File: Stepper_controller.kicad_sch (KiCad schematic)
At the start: 26 parts

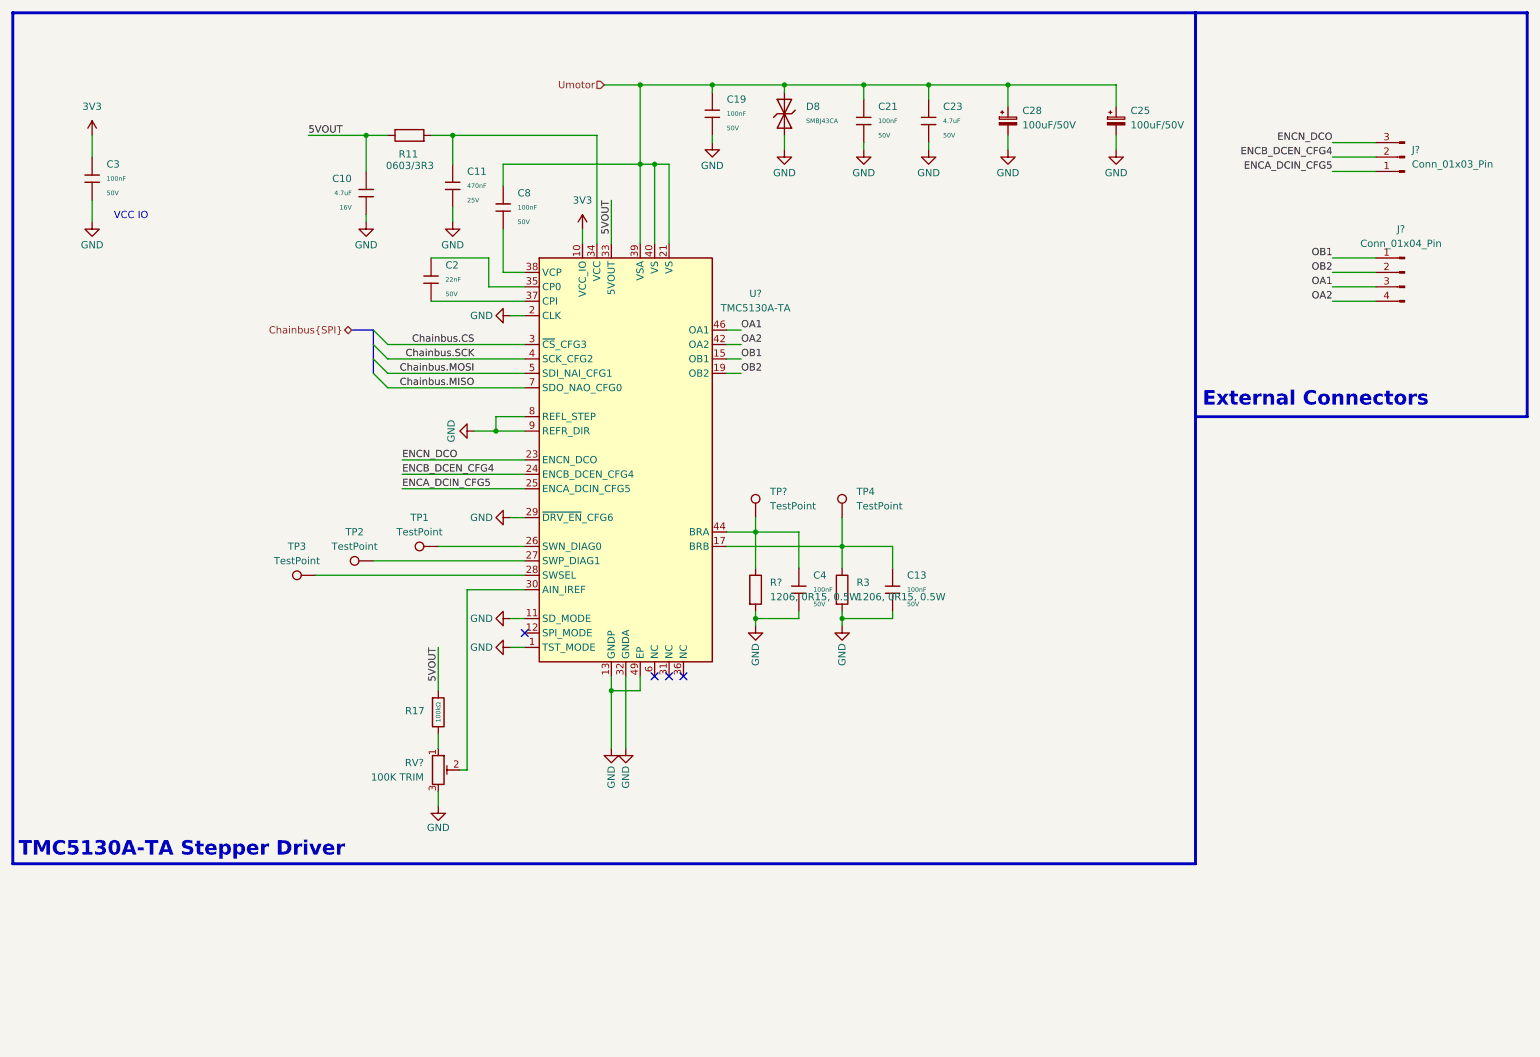
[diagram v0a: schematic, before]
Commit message: finished schematic (without some part numbers)
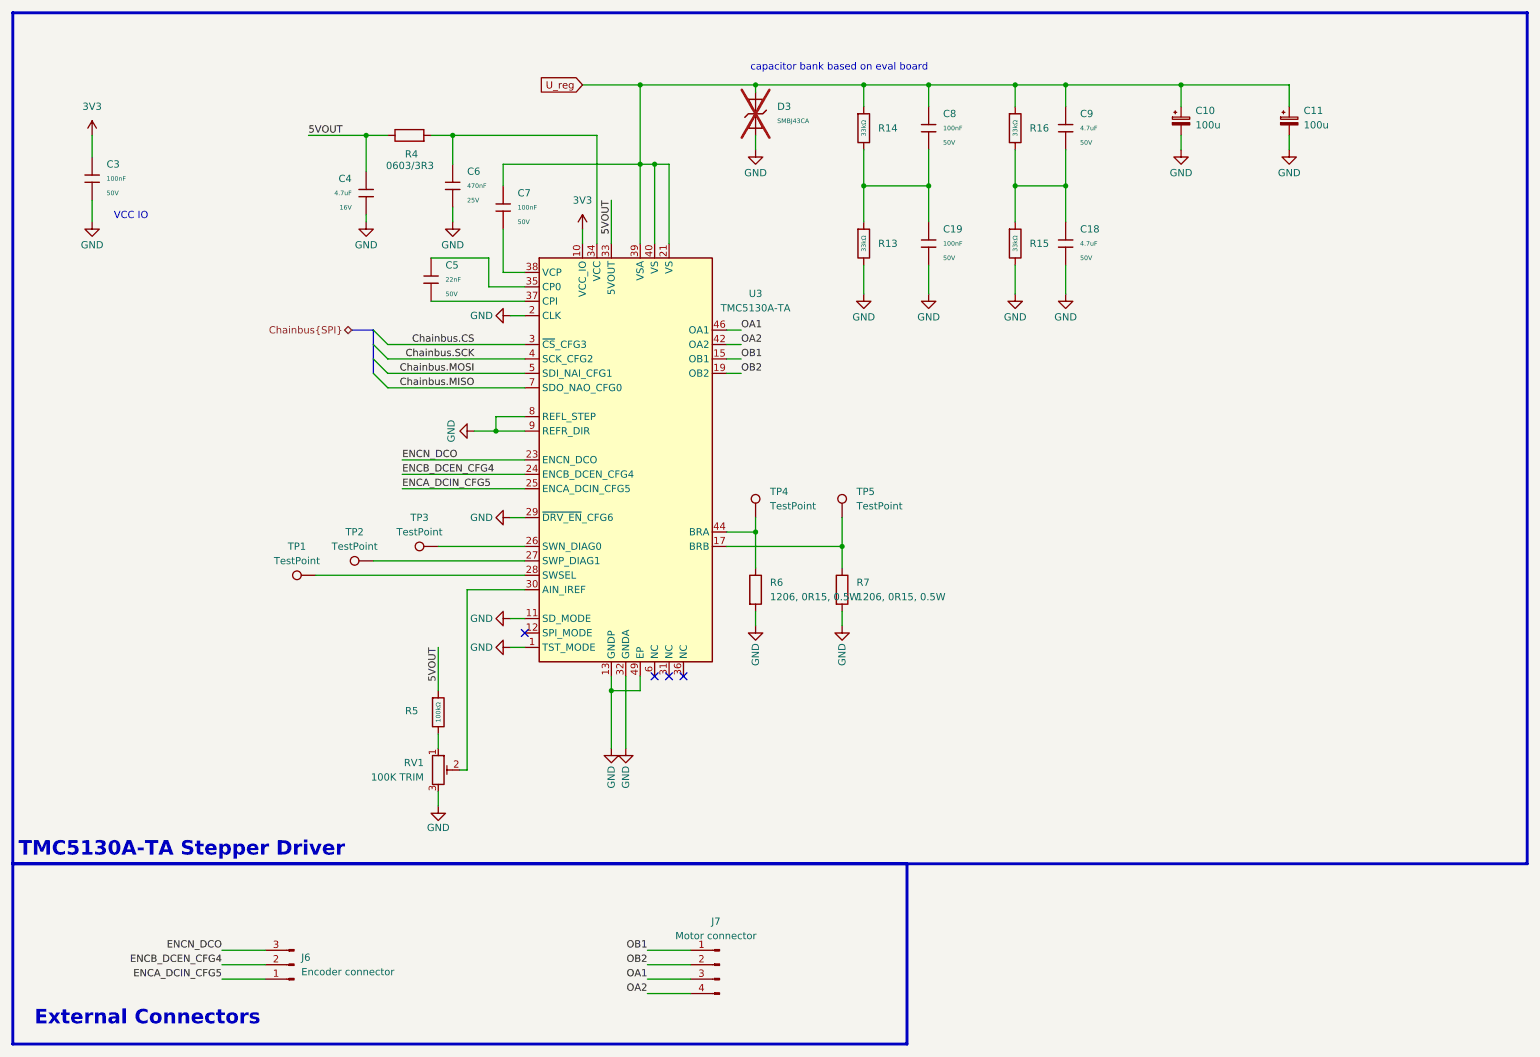
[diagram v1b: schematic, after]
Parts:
- removed C13, C4: 100nF, PCM_JLCPCB:C_0603, symbol PCM_JLCPCB-Capacitors:0603,100nF
- removed C25: 100uF/50V, symbol Device:C_Polarized_Small
- added C11: 100u, Capacitor_SMD:CP_Elec_10x12.5, symbol Device:C_Polarized_Small
- added C18: 4.7uF, PCM_JLCPCB:C_1206, symbol PCM_JLCPCB-Capacitors:1206,4.7uF
- added R13, R14, R15, R16: 33kΩ, PCM_JLCPCB:R_0402, symbol PCM_JLCPCB-Resistors:0402,33kΩ
- C10: renamed from C28; value 100uF/50V -> 100u; footprint (none) -> Capacitor_SMD:CP_Elec_10x12.5; LCSC (none) -> C22387799
- D3: renamed from D8; now not fitted
- J6: renamed from J?; value Conn_01x03_Pin -> Encoder connector
- J7: renamed from J?; value Conn_01x04_Pin -> Motor connector
- gave numbers to parts that had none: 4
- renumbered C10 to C4, C2 to C5, C11 to C6, C8 to C7, C21 to C8, C23 to C9, R11 to R4, R17 to R5, R3 to R7, TP3 to TP1, TP1 to TP3, TP4 to TP5
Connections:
- net GND: now also C11.2, C18.2, R13.2, R15.2; no longer C8.2, C9.2
- net Umotor renamed U_reg
- net U_reg: now also C11.1, R14.1, R16.1; no longer C19.1
- new net: C19.1, C8.2, R13.1, R14.2
- new net: C18.1, C9.2, R15.1, R16.2
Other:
- note added: "capacitor bank based on eval board"
- moved on the sheet: C10, C8, C9, J6, J7

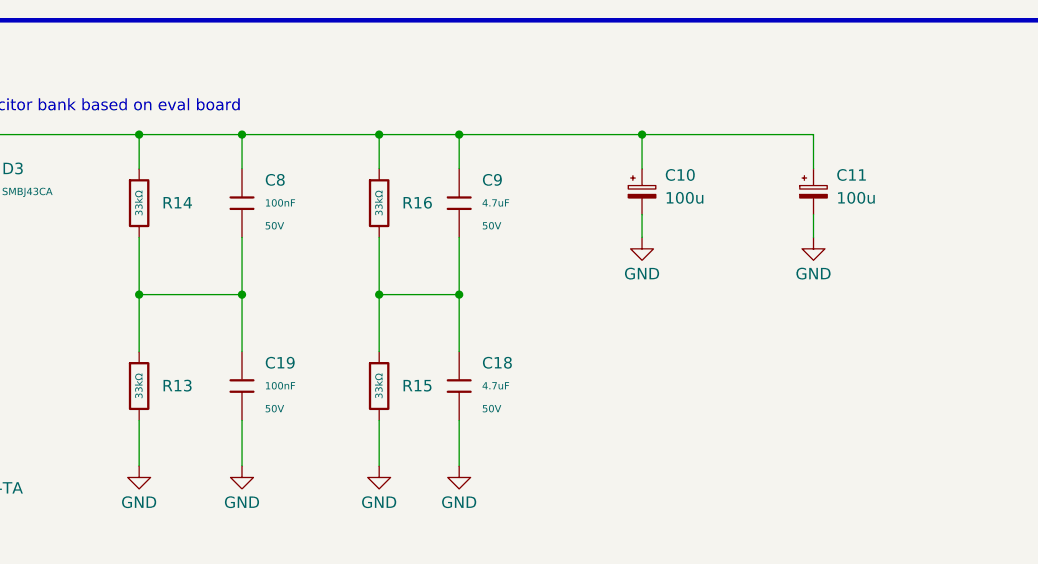
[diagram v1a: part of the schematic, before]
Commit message: initial component placement
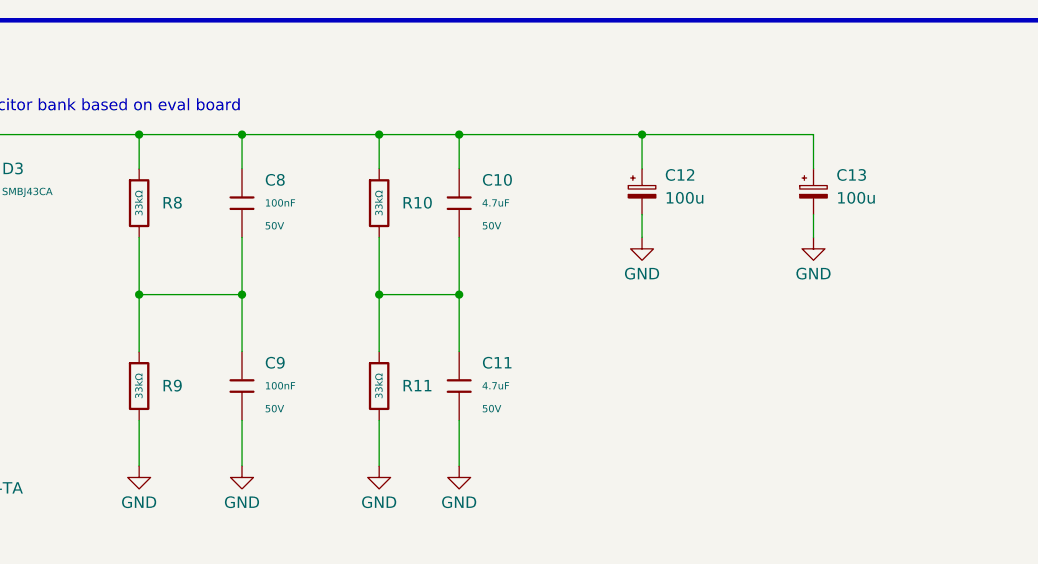
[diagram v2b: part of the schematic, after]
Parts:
- J6: footprint (none) -> Connector_PinHeader_2.54mm:PinHeader_1x03_P2.54mm_Vertical
- J7: footprint (none) -> Connector_PinHeader_2.54mm:PinHeader_1x04_P2.54mm_Vertical
- R4: footprint (none) -> PCM_JLCPCB:R_1206; LCSC (none) -> C911994
- R6, R7: footprint (none) -> PCM_JLCPCB:R_1206; LCSC (none) -> C2683383
- RV1: footprint (none) -> Potentiometer_SMD:Potentiometer_Vishay_TS53YJ_Vertical; LCSC (none) -> C51284
- TP1, TP2, TP3, TP4, TP5: footprint (none) -> TestPoint:TestPoint_Pad_D1.0mm
- renumbered C9 to C10, C18 to C11, C10 to C12, C11 to C13, C19 to C9, R16 to R10, R15 to R11, R14 to R8, R13 to R9
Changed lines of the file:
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@@
 		(on_board yes)
 		(dnp no)
-		(property "Reference" "#PWR081"
+		(property "Reference" "#PWR062"
 			(at 163.83 69.85 0)
 			(effects
@@
 			(project "MMS3_hat_stepper_controler"
 				(path "/6596548a-44e0-46d8-8624-fd71cf4a3e17/08d7247e-6849-4d2d-9ddf-0299da50b957"
-					(reference "#PWR081")
+					(reference "#PWR062")
 					(unit 1)
 				)
@@
 		(on_board yes)
 		(dnp no)
-		(property "Reference" "#PWR065"
+		(property "Reference" "#PWR067"
 			(at 238.76 44.45 0)
 			(effects
@@
 			(project "MMS2_hat_template_small"
 				(path "/6596548a-44e0-46d8-8624-fd71cf4a3e17/08d7247e-6849-4d2d-9ddf-0299da50b957"
-					(reference "#PWR065")
+					(reference "#PWR067")
 					(unit 1)
 				)
@@
 			)
 		)
-		(property "Footprint" ""
+		(property "Footprint" "TestPoint:TestPoint_Pad_D1.0mm"
 			(at 88.9 102.87 0)
 			(effects
@@
 		(on_board yes)
 		(dnp no)
-		(property "Reference" "#PWR061"
+		(property "Reference" "#PWR063"
 			(at 175.26 69.85 0)
 			(effects
@@
 			(project "MMS2_hat_template_small"
 				(path "/6596548a-44e0-46d8-8624-fd71cf4a3e17/08d7247e-6849-4d2d-9ddf-0299da50b957"
-					(reference "#PWR061")
+					(reference "#PWR063")
 					(unit 1)
 				)
@@
 			)
 		)
-		(property "Footprint" ""
+		(property "Footprint" "PCM_JLCPCB:R_1206"
 			(at 158.242 115.57 90)
 			(effects
@@
 			)
 		)
+		(property "LCSC" "C2683383"
+			(at 160.02 115.57 0)
+			(effects
+				(font
+					(size 1.27 1.27)
+				)
+				(hide yes)
+			)
+		)
 		(pin "1"
 		)
@@
 			)
 		)
-		(property "Footprint" ""
+		(property "Footprint" "TestPoint:TestPoint_Pad_D1.0mm"
 			(at 67.31 107.95 0)
 			(effects
@@
 			)
 		)
-		(property "Footprint" ""
+		(property "Footprint" "PCM_JLCPCB:R_1206"
 			(at 143.002 115.57 90)
 			(effects
@@
 			)
 		)
+		(property "LCSC" "C2683383"
+			(at 144.78 115.57 0)
+			(effects
+				(font
+					(size 1.27 1.27)
+				)
+				(hide yes)
+			)
+		)
 		(pin "1"
 		)
@@
 			)
 		)
-		(property "Footprint" ""
+		(property "Footprint" "TestPoint:TestPoint_Pad_D1.0mm"
 			(at 77.47 105.41 0)
 			(effects
@@
 		(on_board yes)
 		(dnp no)
-		(property "Reference" "#PWR063"
+		(property "Reference" "#PWR065"
 			(at 199.39 69.85 0)
 			(effects
@@
 			(project "MMS2_hat_template_small"
 				(path "/6596548a-44e0-46d8-8624-fd71cf4a3e17/08d7247e-6849-4d2d-9ddf-0299da50b957"
-					(reference "#PWR063")
+					(reference "#PWR065")
 					(unit 1)
 				)
@@
 			)
 		)
-		(property "Footprint" ""
+		(property "Footprint" "Connector_PinHeader_2.54mm:PinHeader_1x03_P2.54mm_Vertical"
 			(at 63.5 181.61 0)
 			(effects
@@
 			)
 		)
-		(property "Footprint" ""
+		(property "Footprint" "PCM_JLCPCB:R_1206"
 			(at 83.82 37.338 90)
 			(effects
@@
 			)
 		)
+		(property "LCSC" "C911994"
+			(at 83.82 35.56 90)
+			(effects
+				(font
+					(size 1.27 1.27)
+				)
+				(hide yes)
+			)
+		)
 		(pin "2"
 		)
@@
 		(on_board yes)
 		(dnp no)
-		(property "Reference" "#PWR062"
+		(property "Reference" "#PWR061"
 			(at 160.02 128.27 0)
 			(effects
@@
 			(project "MMS2_hat_template_small"
 				(path "/6596548a-44e0-46d8-8624-fd71cf4a3e17/08d7247e-6849-4d2d-9ddf-0299da50b957"
-					(reference "#PWR062")
+					(reference "#PWR061")
 					(unit 1)
 				)
@@
 			)
 		)
-		(property "Footprint" ""
+		(property "Footprint" "Connector_PinHeader_2.54mm:PinHeader_1x04_P2.54mm_Vertical"
 			(at 138.43 181.61 0)
 			(effects
@@
 		(dnp no)
 		(fields_autoplaced yes)
-		(property "Reference" "R15"
+		(property "Reference" "R11"
 			(at 193.04 54.6099 0)
 			(effects
@@
 			(project "MMS3_hat_stepper_controler"
 				(path "/6596548a-44e0-46d8-8624-fd71cf4a3e17/08d7247e-6849-4d2d-9ddf-0299da50b957"
-					(reference "R15")
+					(reference "R11")
 					(unit 1)
 				)
@@
 			)
 		)
-		(property "Footprint" ""
+		(property "Footprint" "TestPoint:TestPoint_Pad_D1.0mm"
 			(at 149.86 102.87 0)
 			(effects
@@
 		(on_board yes)
 		(dnp no)
-		(property "Reference" "#PWR064"
+		(property "Reference" "#PWR066"
 			(at 219.71 44.45 0)
 			(effects
@@
 			(project "MMS2_hat_template_small"
 				(path "/6596548a-44e0-46d8-8624-fd71cf4a3e17/08d7247e-6849-4d2d-9ddf-0299da50b957"
-					(reference "#PWR064")
+					(reference "#PWR066")
 					(unit 1)
 				)
@@
 		(dnp no)
 		(fields_autoplaced yes)
-		(property "Reference" "C11"
+		(property "Reference" "C13"
 			(at 241.3 31.2038 0)
 			(effects
@@
 			(project "MMS3_hat_stepper_controler"
 				(path "/6596548a-44e0-46d8-8624-fd71cf4a3e17/08d7247e-6849-4d2d-9ddf-0299da50b957"
-					(reference "C11")
+					(reference "C13")
 					(unit 1)
 				)
@@
 		(dnp no)
 		(fields_autoplaced yes)
-		(property "Reference" "C18"
+		(property "Reference" "C11"
 			(at 201.93 52.0699 0)
 			(effects
@@
 			(project "MMS3_hat_stepper_controler"
 				(path "/6596548a-44e0-46d8-8624-fd71cf4a3e17/08d7247e-6849-4d2d-9ddf-0299da50b957"
-					(reference "C18")
+					(reference "C11")
 					(unit 1)
 				)
@@
 			)
 		)
-		(property "Footprint" ""
+		(property "Footprint" "Potentiometer_SMD:Potentiometer_Vishay_TS53YJ_Vertical"
 			(at 88.9 147.32 0)
 			(effects
@@
 			)
 		)
+		(property "LCSC" "C51284"
+			(at 88.9 147.32 0)
+			(effects
+				(font
+					(size 1.27 1.27)
+				)
+				(hide yes)
+			)
+		)
 		(pin "2"
 		)
@@
 		(dnp no)
 		(fields_autoplaced yes)
-		(property "Reference" "R14"
+		(property "Reference" "R8"
 			(at 166.37 34.2899 0)
 			(effects
@@
 			(project ""
 				(path "/6596548a-44e0-46d8-8624-fd71cf4a3e17/08d7247e-6849-4d2d-9ddf-0299da50b957"
-					(reference "R14")
+					(reference "R8")
 					(unit 1)
 				)
@@
 		(dnp no)
 		(fields_autoplaced yes)
-		(property "Reference" "C10"
+		(property "Reference" "C12"
 			(at 222.25 31.2038 0)
 			(effects
@@
 			(project ""
 				(path "/6596548a-44e0-46d8-8624-fd71cf4a3e17/08d7247e-6849-4d2d-9ddf-0299da50b957"
-					(reference "C10")
+					(reference "C12")
 					(unit 1)
 				)
@@
 		(on_board yes)
 		(dnp no)
-		(property "Reference" "#PWR080"
+		(property "Reference" "#PWR064"
 			(at 190.5 69.85 0)
 			(effects
@@
 			(project "MMS3_hat_stepper_controler"
 				(path "/6596548a-44e0-46d8-8624-fd71cf4a3e17/08d7247e-6849-4d2d-9ddf-0299da50b957"
-					(reference "#PWR080")
+					(reference "#PWR064")
 					(unit 1)
 				)
@@
 		(dnp no)
 		(fields_autoplaced yes)
-		(property "Reference" "R13"
+		(property "Reference" "R9"
 			(at 166.37 54.6099 0)
 			(effects
@@
 			(project "MMS3_hat_stepper_controler"
 				(path "/6596548a-44e0-46d8-8624-fd71cf4a3e17/08d7247e-6849-4d2d-9ddf-0299da50b957"
-					(reference "R13")
+					(reference "R9")
 					(unit 1)
 				)
@@
 			)
 		)
-		(property "Footprint" ""
+		(property "Footprint" "TestPoint:TestPoint_Pad_D1.0mm"
 			(at 165.1 102.87 0)
 			(effects
@@
 		(dnp no)
 		(fields_autoplaced yes)
-		(property "Reference" "R16"
+		(property "Reference" "R10"
 			(at 193.04 34.2899 0)
 			(effects
@@
 			(project "MMS3_hat_stepper_controler"
 				(path "/6596548a-44e0-46d8-8624-fd71cf4a3e17/08d7247e-6849-4d2d-9ddf-0299da50b957"
-					(reference "R16")
+					(reference "R10")
 					(unit 1)
 				)
@@
 		(dnp no)
 		(fields_autoplaced yes)
-		(property "Reference" "C19"
+		(property "Reference" "C9"
 			(at 177.8 52.0699 0)
 			(effects
@@
 			(project "MMS3_hat_stepper_controler"
 				(path "/6596548a-44e0-46d8-8624-fd71cf4a3e17/08d7247e-6849-4d2d-9ddf-0299da50b957"
-					(reference "C19")
+					(reference "C9")
 					(unit 1)
 				)
@@
 		(dnp no)
 		(fields_autoplaced yes)
-		(property "Reference" "C9"
+		(property "Reference" "C10"
 			(at 201.93 31.7499 0)
 			(effects
@@
 			(project ""
 				(path "/6596548a-44e0-46d8-8624-fd71cf4a3e17/08d7247e-6849-4d2d-9ddf-0299da50b957"
-					(reference "C9")
+					(reference "C10")
 					(unit 1)
 				)

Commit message: revision
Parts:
- removed R10, R11: 33kΩ, PCM_JLCPCB:R_0402, symbol PCM_JLCPCB-Resistors:0402,33kΩ
- added C14, C15: 100u, Capacitor_SMD:CP_Elec_10x12.5, symbol Device:C_Polarized_Small
- added TP6: TestPoint, TestPoint:TestPoint_Pad_D1.0mm, symbol Connector:TestPoint
- J6: footprint Connector_PinHeader_2.54mm:PinHeader_1x03_P2.54mm_Vertical -> Connector_JST:JST_XH_S3B-XH-A-1_1x03_P2.50mm_Horizontal
- J7: footprint Connector_PinHeader_2.54mm:PinHeader_1x04_P2.54mm_Vertical -> Connector_JST:JST_XH_S4B-XH-A_1x04_P2.50mm_Horizontal
- RV1: footprint Potentiometer_SMD:Potentiometer_Vishay_TS53YJ_Vertical -> Potentiometer_THT:Potentiometer_Bourns_3386W_Horizontal; LCSC C51284 -> C48084
- U3: LCSC (none) -> C188832
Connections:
- net GND: now also C14.2, C15.2
- net U_reg: now also C14.1, C15.1
- net at RV1.2, U3.30 (AIN_IREF): now also TP6.1
- net at C8.2, C9.1, R8.2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: now also C10.2, C11.1
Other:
- moved on the sheet: C10, C11

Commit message: second component placement
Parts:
- C12, C13, C14, C15: value 100u -> 47u; footprint Capacitor_SMD:CP_Elec_10x12.5 -> Capacitor_SMD:CP_Elec_6.3x7.7; LCSC C22387799 -> C7461235
- RV1: footprint Potentiometer_THT:Potentiometer_Bourns_3386W_Horizontal -> Potentiometer_THT:Potentiometer_Bourns_3296W_Vertical; LCSC C48084 -> C48641782
- renumbered TP6 to TP4, TP4 to TP5, TP5 to TP6
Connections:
- net OA1: now also J7.1 (Pin_1); no longer J7.3 (Pin_3)
- net OA2: now also J7.2 (Pin_2); no longer J7.4 (Pin_4)
- net OB1: now also J7.3 (Pin_3); no longer J7.1 (Pin_1)
- net OB2: now also J7.4 (Pin_4); no longer J7.2 (Pin_2)
- net 3V3 renamed +3V3
